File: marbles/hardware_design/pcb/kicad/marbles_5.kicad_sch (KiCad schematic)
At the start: 60 parts

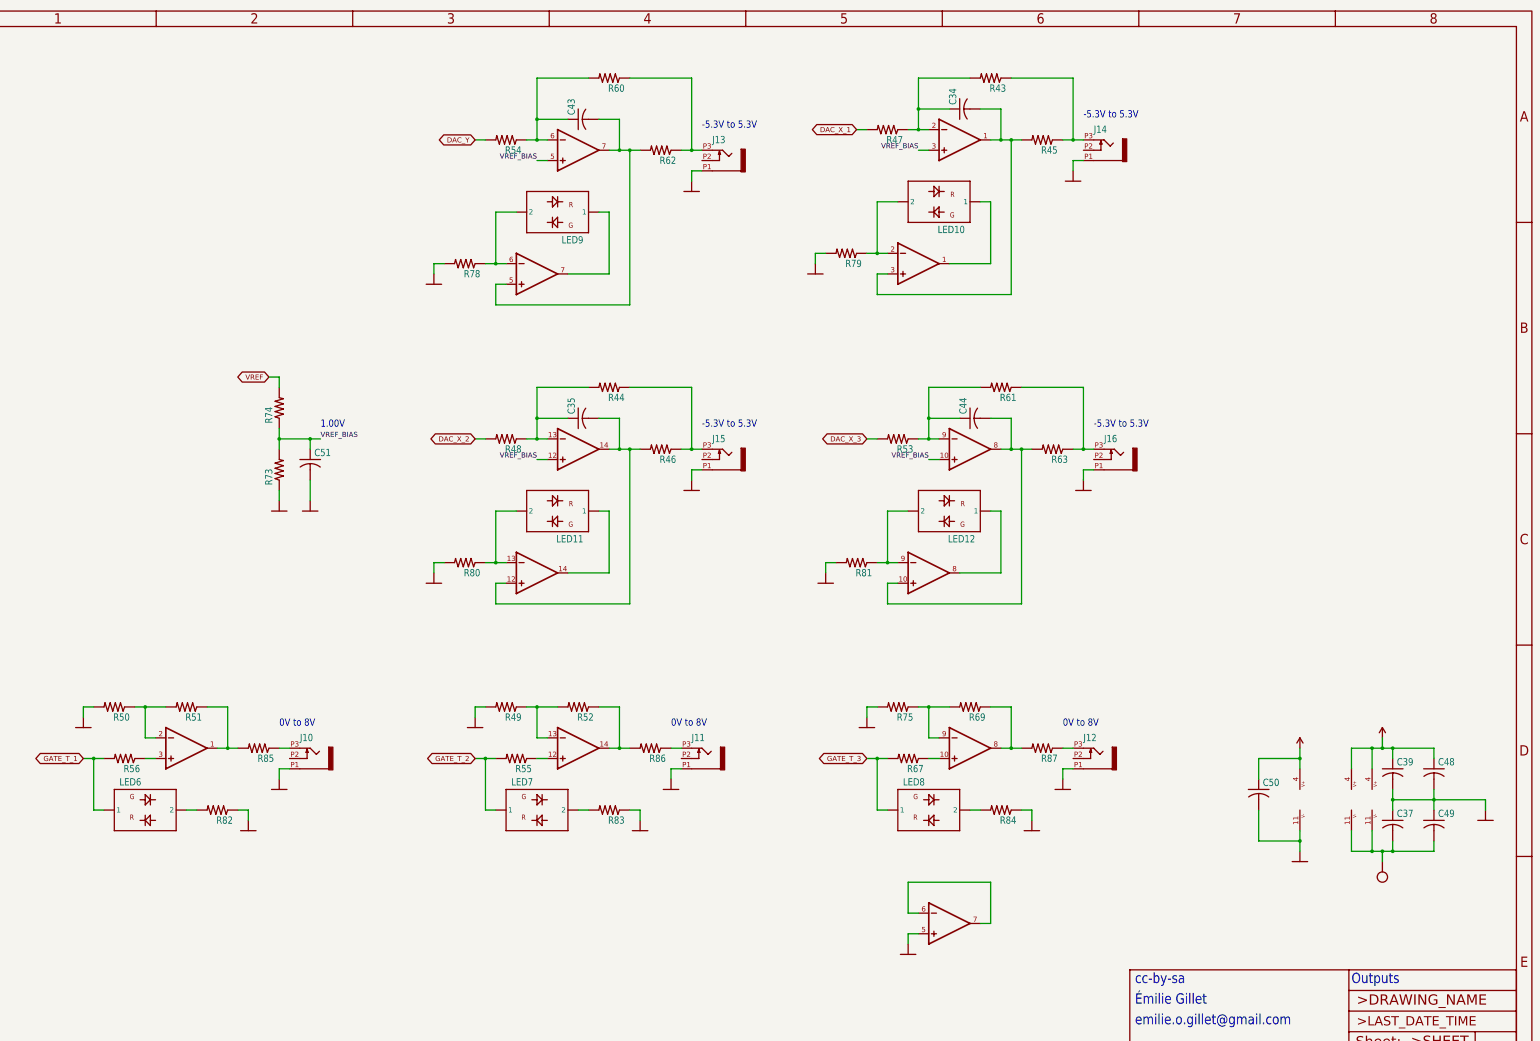
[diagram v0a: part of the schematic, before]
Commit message: added SMD LEDs in parallel with THT footprint
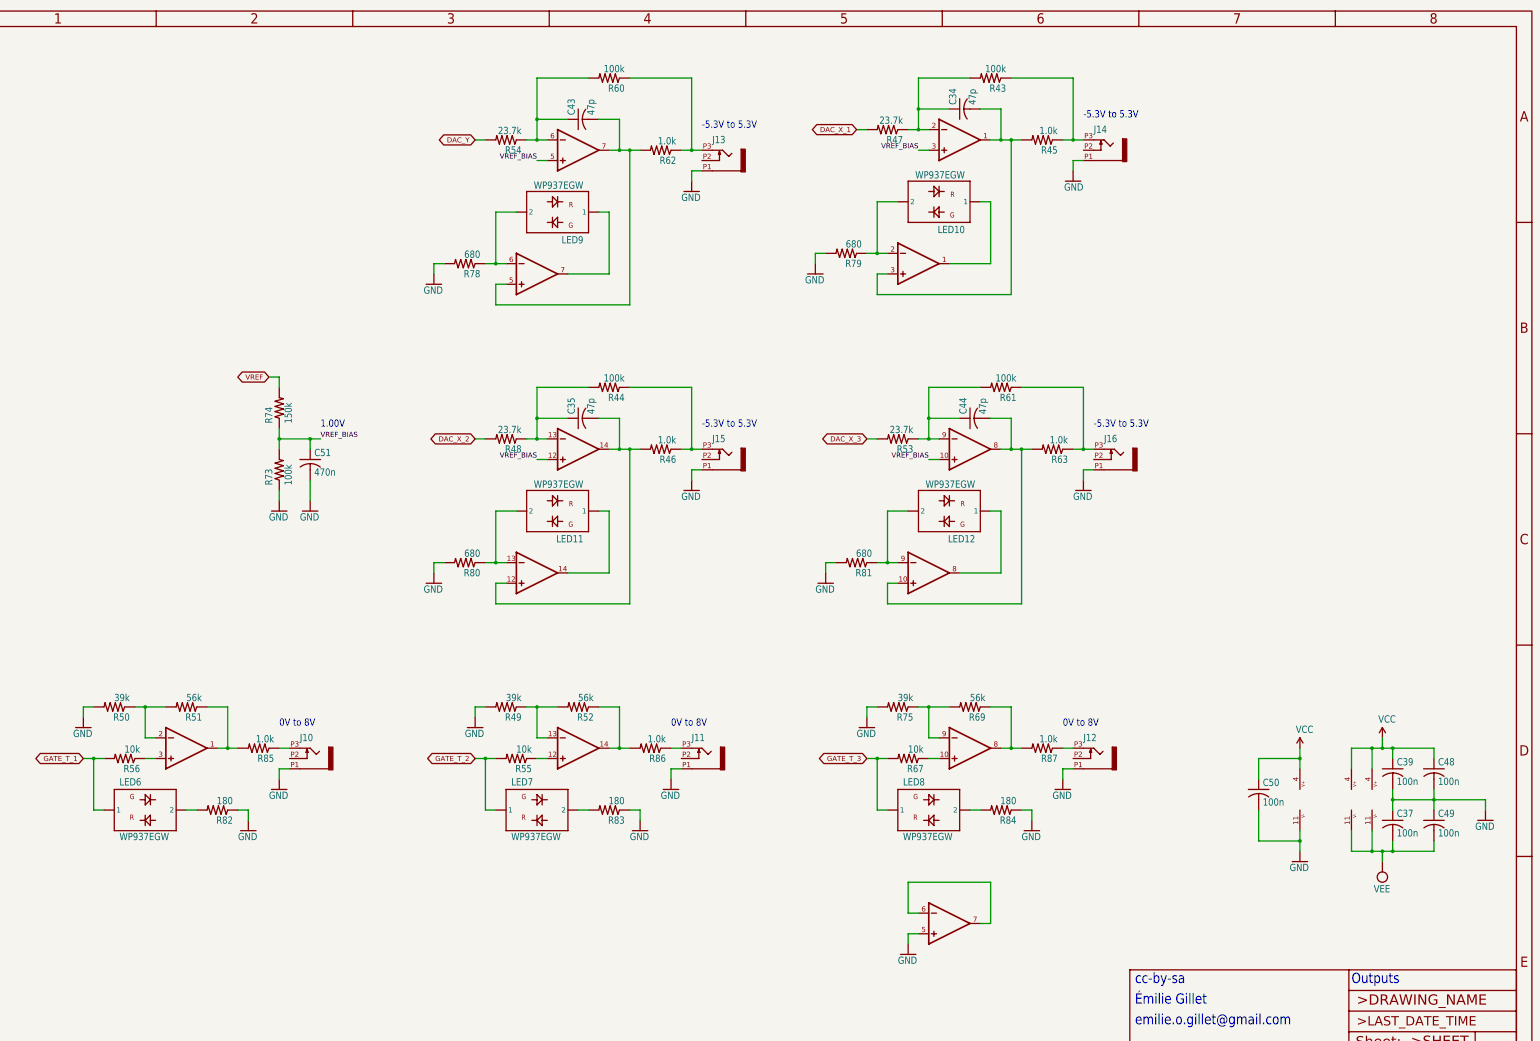
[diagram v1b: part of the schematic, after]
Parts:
- C34, C35, C43, C44: value (none) -> 47p; footprint (none) -> marbles:C0402
- C37, C39, C48, C49, C50: value (none) -> 100n; footprint (none) -> marbles:C0402
- C51: value (none) -> 470n; footprint (none) -> marbles:C0402
- IC10: value (none) -> TL074PW; footprint (none) -> marbles:TSSOP14_065
- IC7: value (none) -> OPA4171; footprint (none) -> marbles:TSSOP14_065
- IC9: value (none) -> LM324PW; footprint (none) -> marbles:TSSOP14_065
- J10, J11, J12, J13, J14, J15, J16: value (none) -> PJ301_THONKICONN6; footprint (none) -> marbles:WQP_PJ_301M6
- LED10, LED11, LED12, LED6, LED7, LED8, LED9: value (none) -> WP937EGW; footprint (none) -> marbles:LED3MM
- R43, R44, R60, R61, R73: value (none) -> 100k; footprint (none) -> marbles:R0402
- R45, R46, R62, R63, R85, R86, R87: value (none) -> 1.0k; footprint (none) -> marbles:R0603
- R47, R48, R53, R54: value (none) -> 23.7k; footprint (none) -> marbles:R0402
- R49, R50, R75: value (none) -> 39k; footprint (none) -> marbles:R0402
- R51, R52, R69: value (none) -> 56k; footprint (none) -> marbles:R0402
- R55, R56, R67: value (none) -> 10k; footprint (none) -> marbles:R0402
- R74: value (none) -> 150k; footprint (none) -> marbles:R0402
- R78, R79, R80, R81: value (none) -> 680; footprint (none) -> marbles:R0402
- R82, R83, R84: value (none) -> 180; footprint (none) -> marbles:R0402

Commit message: bottom row output LEDs to SMD
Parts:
- added LED10-2, LED11-2, LED12-2, LED6-2, LED7-2, LED8-2, LED9-2: LED_Dual_KAKA, Supercell 1.3:bicolor 0606 LED, symbol Device:LED_Dual_KAKA
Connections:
- net GATE_T_1: now also LED6-2.AG, LED6-2.KR
- net GATE_T_2: now also LED7-2.AG, LED7-2.KR
- net GATE_T_3: now also LED8-2.AG, LED8-2.KR
- net at IC10.13 (-IN), LED11.2, R80.1: now also LED11-2.AR, LED11-2.KG
- net at LED7.2, R83.2: now also LED7-2.AR, LED7-2.KG
- net at IC10.14 (OUT), LED11.1: now also LED11-2.AG, LED11-2.KR
- net at IC10.8 (OUT), LED12.1: now also LED12-2.AG, LED12-2.KR
- net at IC10.9 (-IN), LED12.2, R81.1: now also LED12-2.AR, LED12-2.KG
- net at IC10.6 (-IN), LED9.2, R78.1: now also LED9-2.AR, LED9-2.KG
- net at LED8.2, R84.2: now also LED8-2.AR, LED8-2.KG
- net at LED6.2, R82.2: now also LED6-2.AR, LED6-2.KG
- net at IC10.1 (OUT), LED10.1: now also LED10-2.AG, LED10-2.KR
- net at IC10.2 (-IN), LED10.2, R79.1: now also LED10-2.AR, LED10-2.KG
- net at IC10.7 (OUT), LED9.1: now also LED9-2.AG, LED9-2.KR
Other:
- moved on the sheet: LED10, LED11, LED12, LED9, R78, R79, R80, R81

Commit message: changed opa4174 package
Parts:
- IC7: footprint marbles:TSSOP14_065 -> Package_SO:SO-14_3.9x8.65mm_P1.27mm
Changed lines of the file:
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@@
       (effects (font (size 1.778 1.5113)) (justify left bottom) hide)
     )
-    (property "Footprint" "marbles:TSSOP14_065" (id 2) (at 170.18 53.34 0)
+    (property "Footprint" "Package_SO:SO-14_3.9x8.65mm_P1.27mm" (id 2) (at 170.18 53.34 0)
       (effects (font (size 1.27 1.27)) hide)
     )
@@
       (effects (font (size 1.778 1.5113)) (justify left bottom) hide)
     )
-    (property "Footprint" "marbles:TSSOP14_065" (id 2) (at 266.7 127 0)
+    (property "Footprint" "Package_SO:SO-14_3.9x8.65mm_P1.27mm" (id 2) (at 266.7 127 0)
       (effects (font (size 1.27 1.27)) hide)
     )
@@
       (effects (font (size 1.778 1.5113)) (justify left bottom) hide)
     )
-    (property "Footprint" "marbles:TSSOP14_065" (id 2) (at 264.16 50.8 0)
+    (property "Footprint" "Package_SO:SO-14_3.9x8.65mm_P1.27mm" (id 2) (at 264.16 50.8 0)
       (effects (font (size 1.27 1.27)) hide)
     )
@@
       (effects (font (size 1.778 1.5113)) (justify left bottom) hide)
     )
-    (property "Footprint" "marbles:TSSOP14_065" (id 2) (at 170.18 127 0)
+    (property "Footprint" "Package_SO:SO-14_3.9x8.65mm_P1.27mm" (id 2) (at 170.18 127 0)
       (effects (font (size 1.27 1.27)) hide)
     )
@@
       (effects (font (size 1.778 1.5113)) (justify left bottom) hide)
     )
-    (property "Footprint" "marbles:TSSOP14_065" (id 2) (at 365.76 213.36 0)
-      (effects (font (size 1.27 1.27)) hide)
-    )
+    (property "Footprint" "Package_SO:SO-14_3.9x8.65mm_P1.27mm" (id 2) (at 365.76 213.36 0)
+      (effects (font (size 1.27 1.27)) hide)
+    )

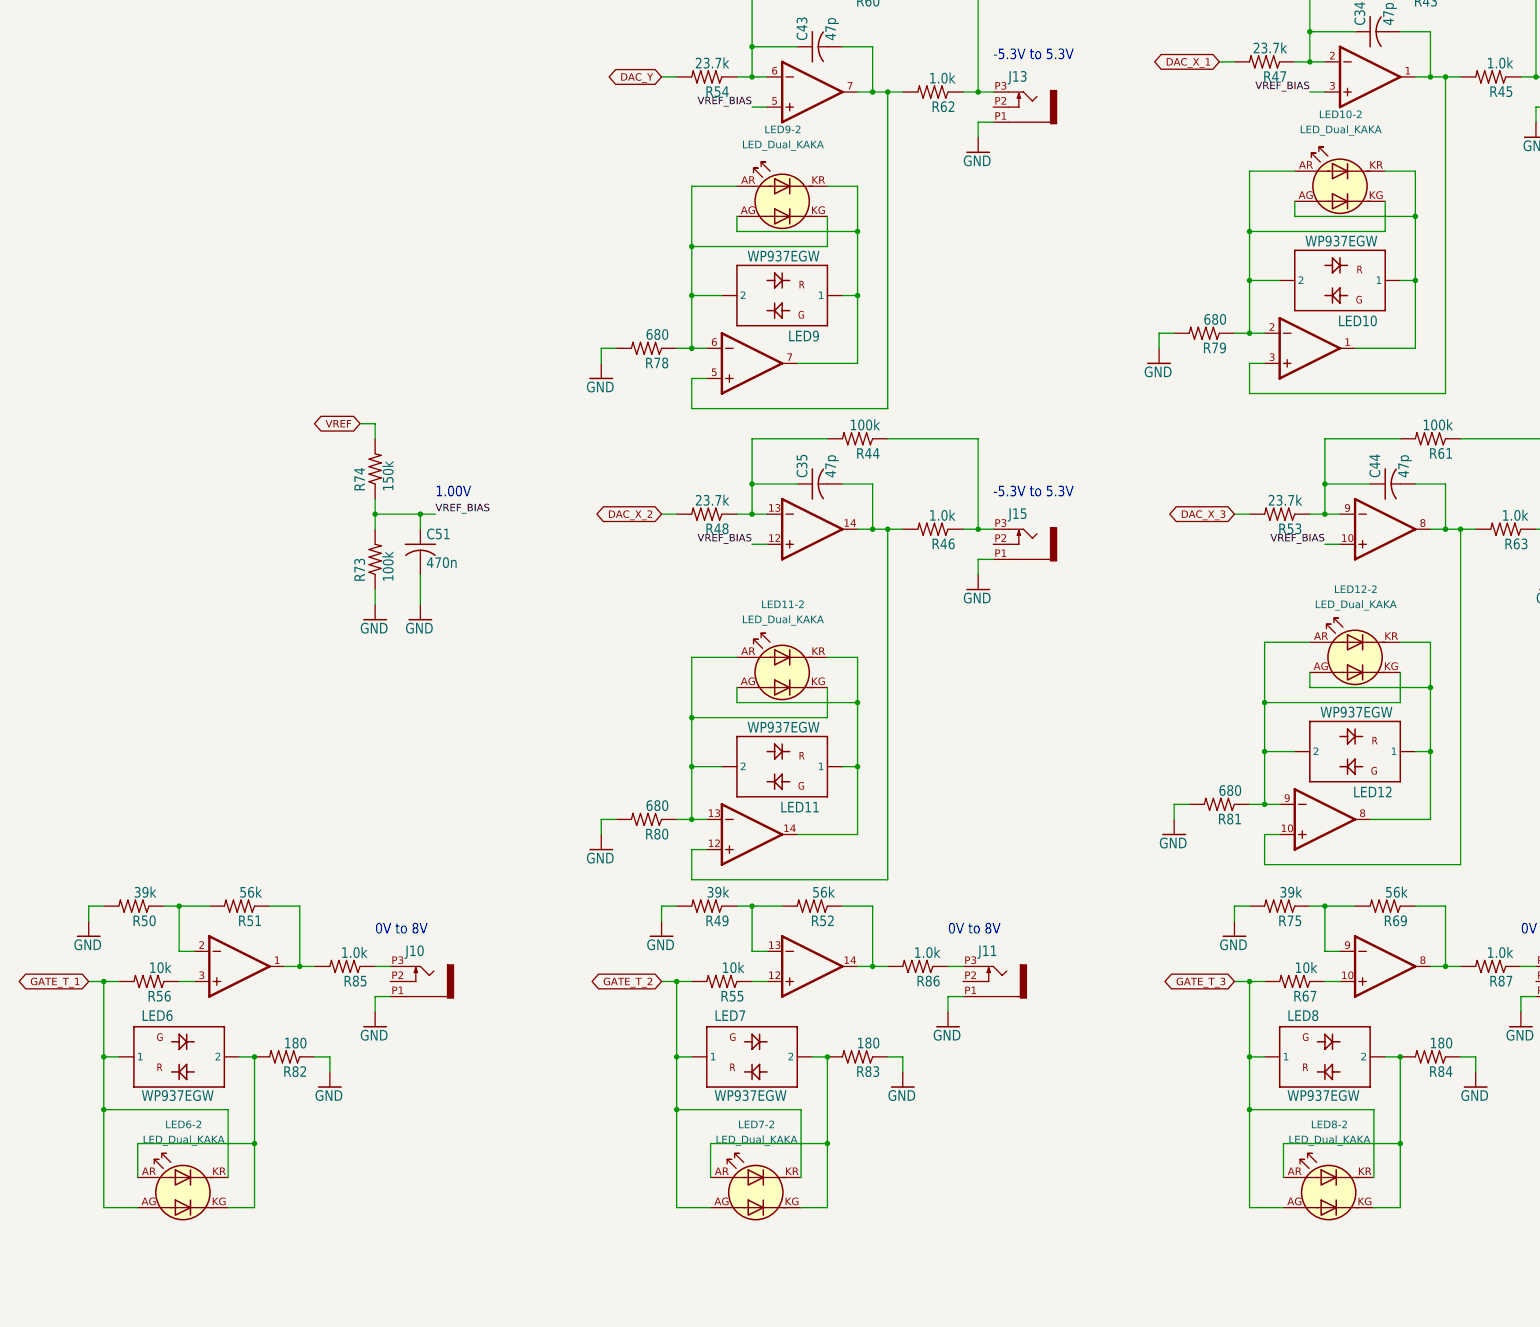
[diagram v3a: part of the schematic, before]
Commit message: marbles remove SMD LEDs, revert to THT
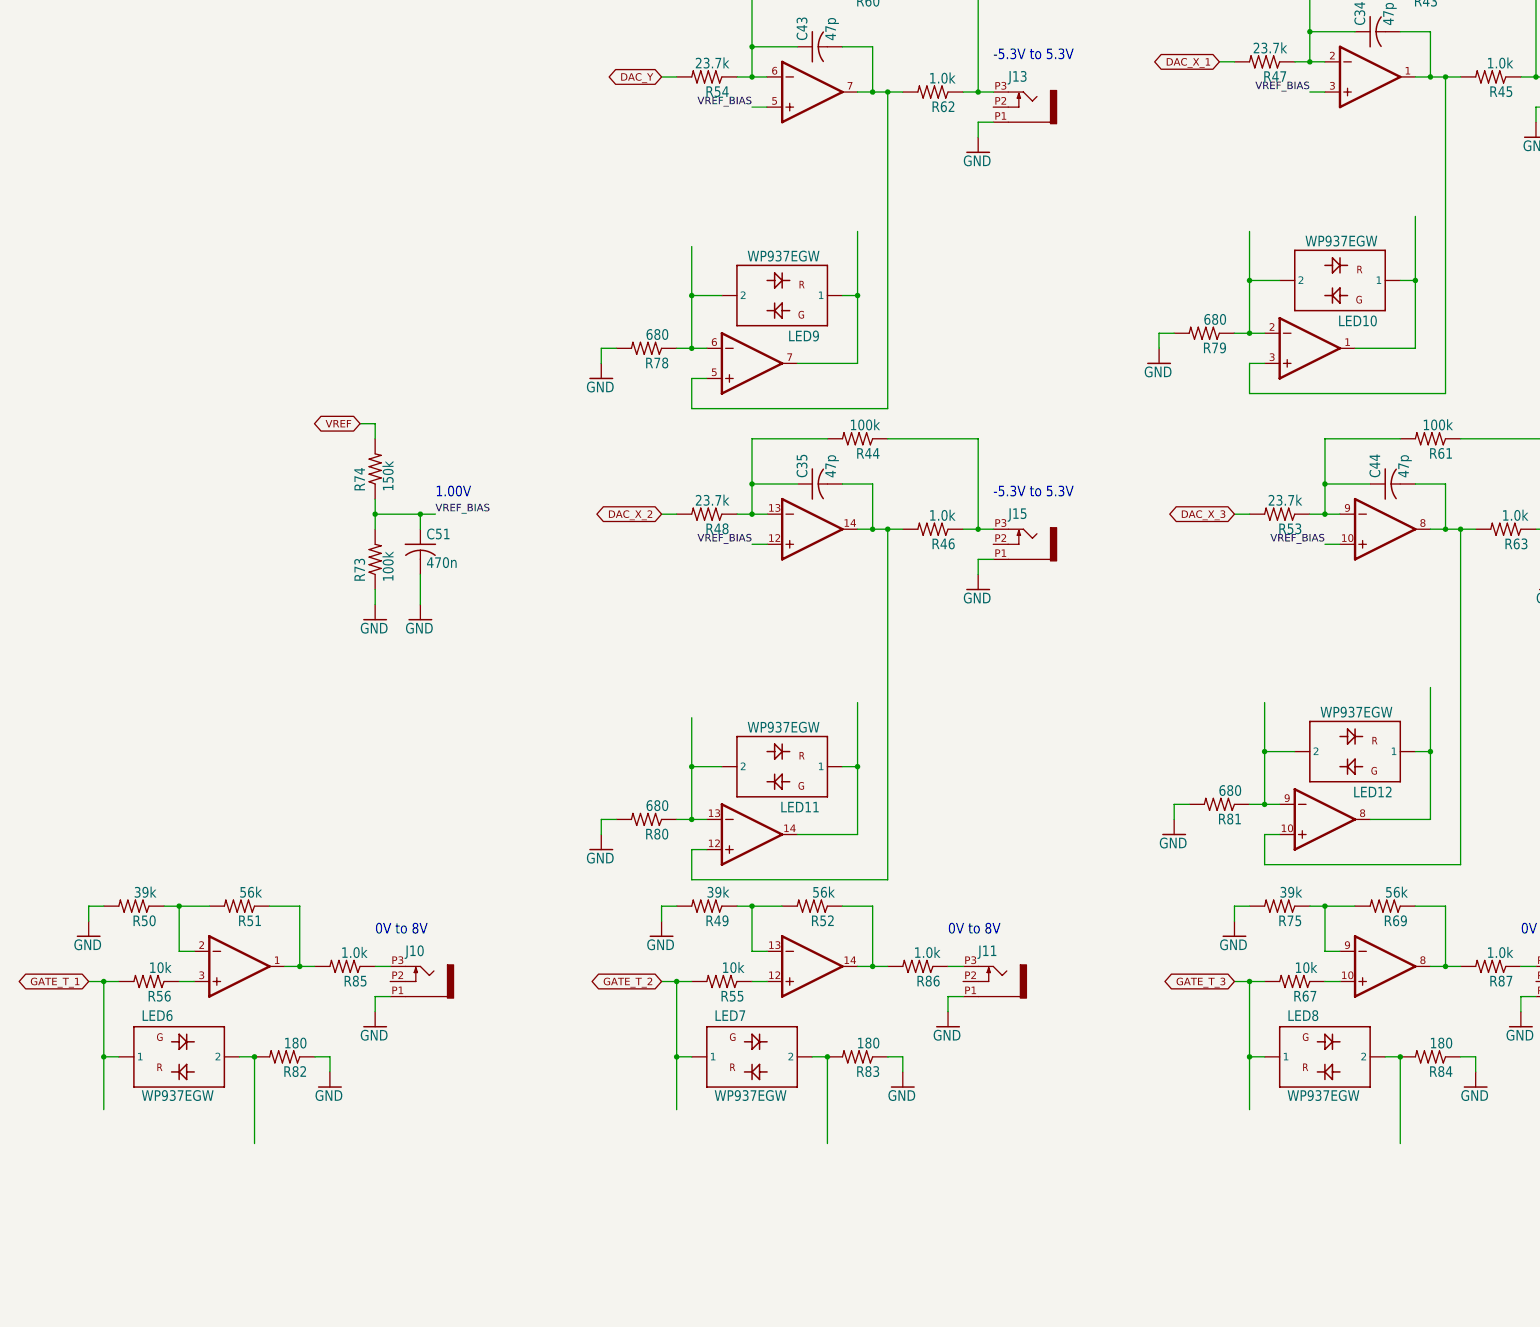
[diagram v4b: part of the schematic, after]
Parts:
- removed LED10-2, LED11-2, LED12-2, LED6-2, LED7-2, LED8-2, LED9-2: LED_Dual_KAKA, Supercell 1.3:bicolor 0606 LED, symbol Device:LED_Dual_KAKA
